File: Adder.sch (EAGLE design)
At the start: 44 parts, among them Q1 MOSFET-NCHANNEL2N7000, Q2 MOSFET-NCHANNEL2N7000, Q3 MOSFET-NCHANNEL2N7000, Q4 MOSFET-NCHANNEL2N7000, Q5 MOSFET-NCHANNEL2N7000, U1 LMS8117, U2 CD74HC283

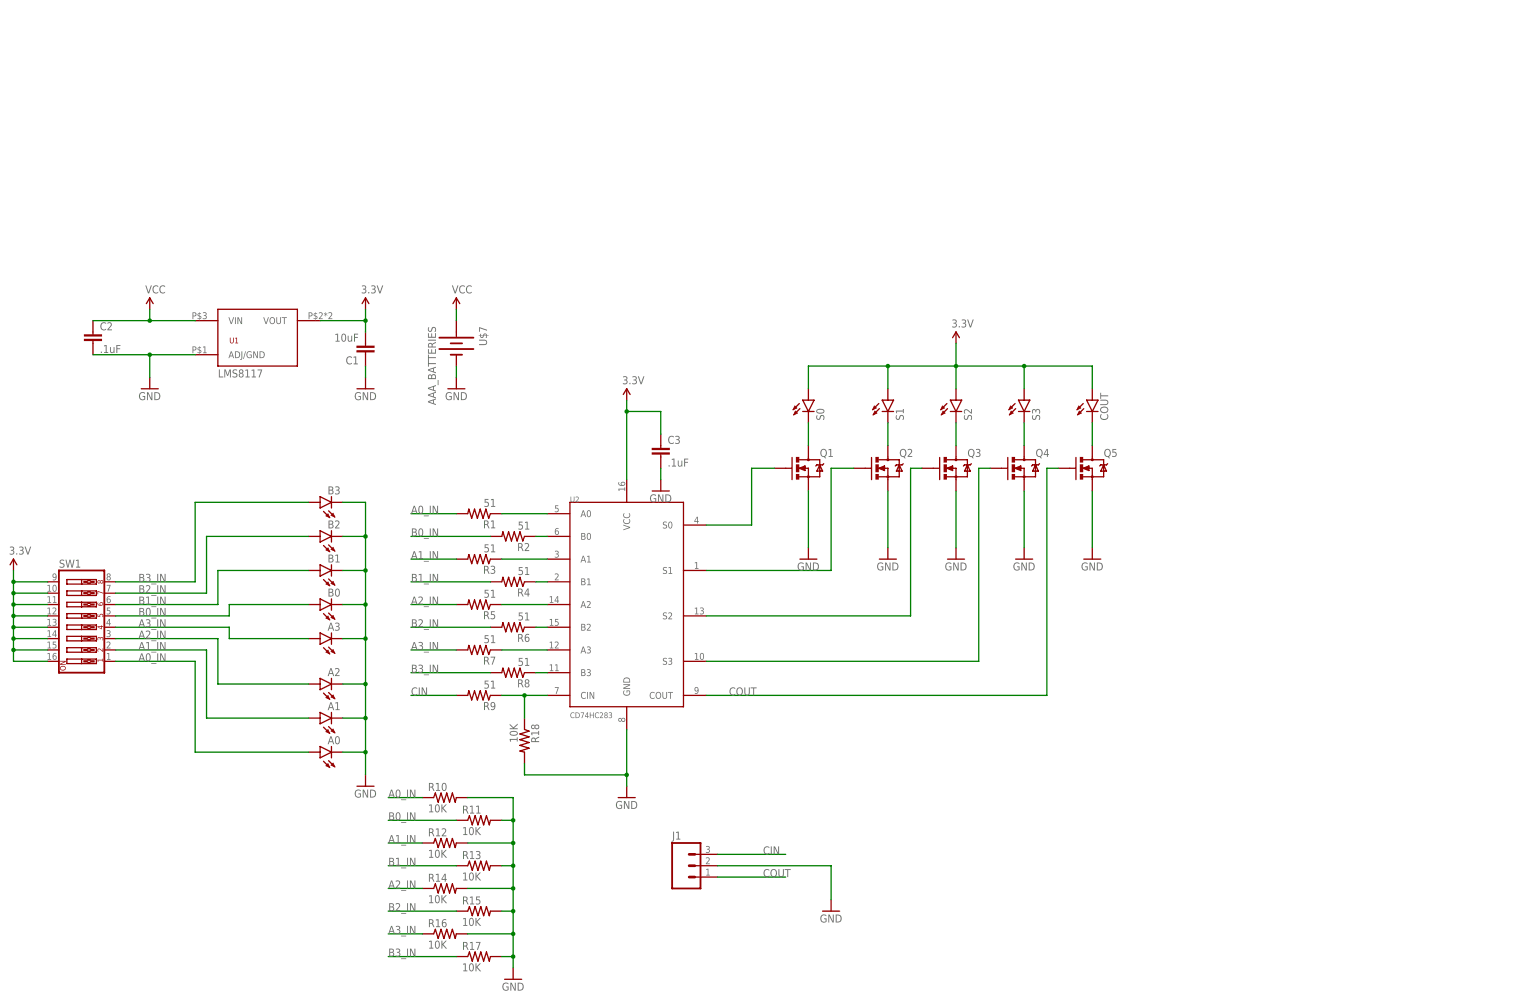
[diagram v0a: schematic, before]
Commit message: Labels for resistor values
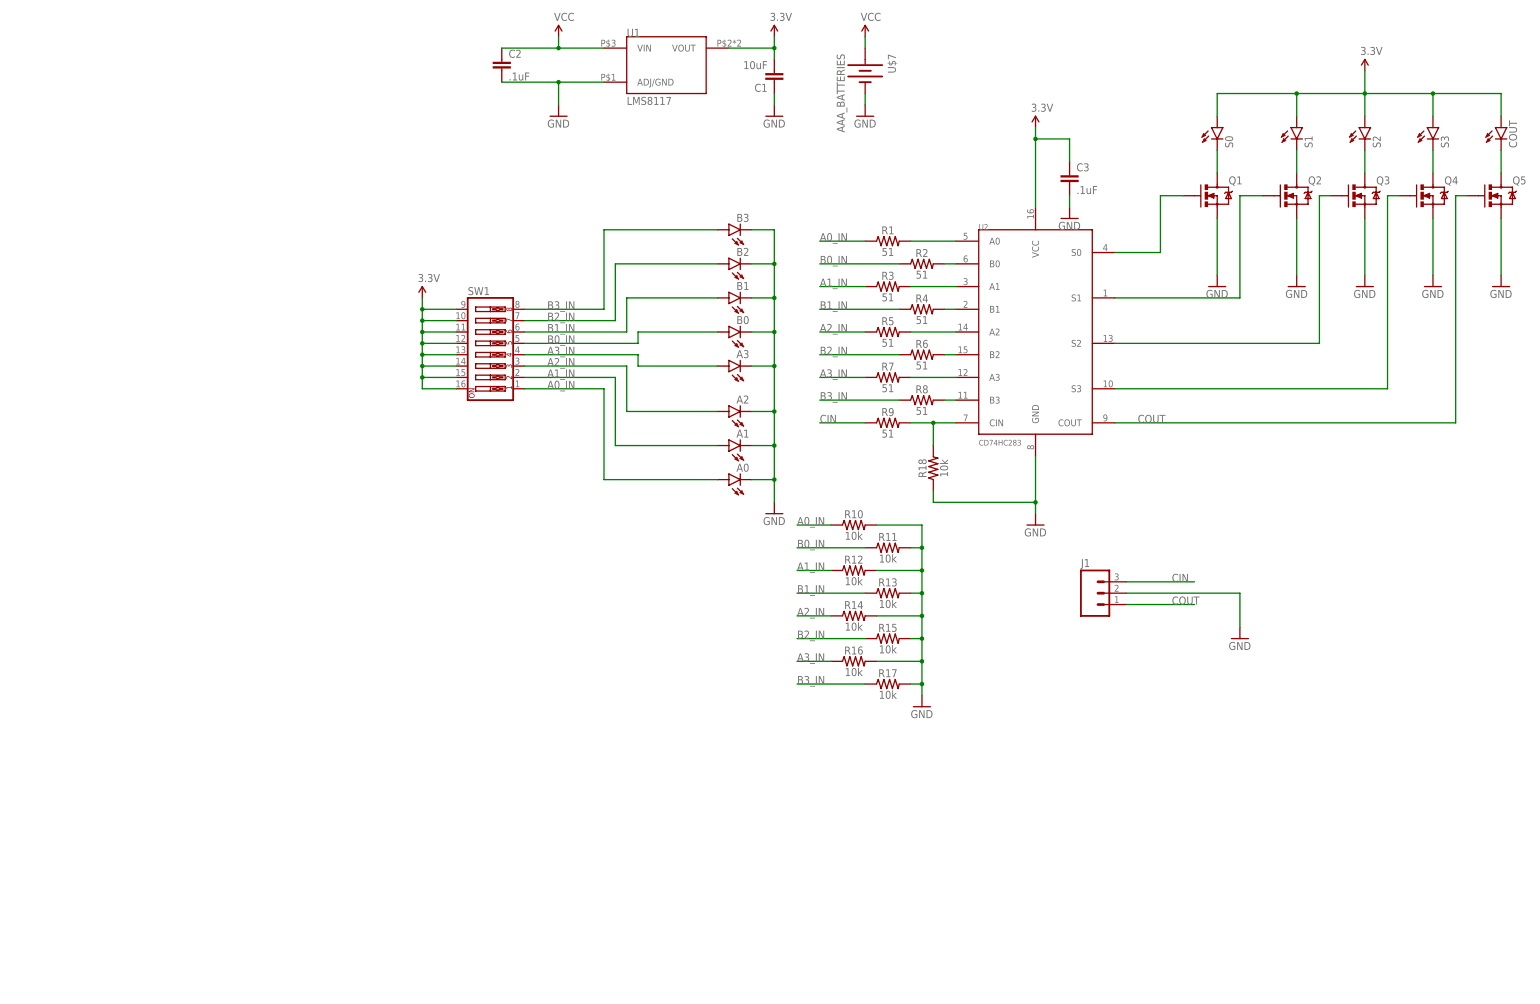
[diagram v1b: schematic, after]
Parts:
- R1, R2, R3, R4, R5, R6, R7, R8, R9: device SparkFun-Resistors:RESISTOR0805-RES -> SparkFun-Resistors:RESISTOR0805
- R10, R11, R12, R13, R14, R15, R16, R17, R18: value 10K -> 10k; device SparkFun-Resistors:RESISTOR0805-RES -> SparkFun-Resistors:RESISTOR0805
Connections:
- net A0_IN: now also R1.1; no longer R1.2
- net A1_IN: now also R3.1; no longer R3.2
- net A2_IN: now also R5.1; no longer R5.2
- net A3_IN: now also R7.1; no longer R7.2
- net B0_IN: now also R2.1; no longer R2.2
- net B1_IN: now also R4.1; no longer R4.2
- net B2_IN: now also R6.1; no longer R6.2
- net B3_IN: now also R8.1; no longer R8.2
- net CIN: now also R9.1; no longer R9.2
- net GND: now also R18.1; no longer R18.2
- net N$32: now also R1.2; no longer R1.1
- net N$33: now also R2.2; no longer R2.1
- net N$34: now also R3.2; no longer R3.1
- net N$35: now also R4.2; no longer R4.1
- net N$36: now also R5.2; no longer R5.1
- net N$37: now also R6.2; no longer R6.1
- net N$38: now also R7.2; no longer R7.1
- net N$39: now also R8.2; no longer R8.1
- net N$40: now also R18.2, R9.2; no longer R18.1, R9.1
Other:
- moved on the sheet: A0, A1, A2, A3, B0, B1, B2, B3, C1, C2, C3, COUT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
